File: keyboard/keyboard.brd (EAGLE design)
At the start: 114 x 132 mm, 47 parts, among them SW1 CHERRY_MX, SW10 CHERRY_MX, SW11 CHERRY_MX, SW12 CHERRY_MX, SW13 CHERRY_MX, SW14 CHERRY_MX, SW15 CHERRY_MX, SW16 CHERRY_MX, SW17 CHERRY_MX, SW18 CHERRY_MX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

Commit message: remove airwire
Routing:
- net GND: track 120.1 -> 112.2 mm
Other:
- outline, holes or cut-outs redrawn
- board text removed: "TODO: Make battery hole"
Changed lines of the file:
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@@
 <setting verticaltext="up"/>
 </settings>
-<grid distance="0.1" unitdist="mm" unit="mm" style="lines" multiple="1" display="yes" altdistance="5" altunitdist="mil" altunit="mil"/>
+<grid distance="0.05" unitdist="mm" unit="mm" style="lines" multiple="1" display="yes" altdistance="5" altunitdist="mil" altunit="mil"/>
 <layers>
 <layer number="1" name="Top" color="4" fill="1" visible="yes" active="yes"/>
@@
 <wire x1="94" y1="122.5" x2="95" y2="121.5" width="0.15" layer="20" curve="-90"/>
 <wire x1="95" y1="121.5" x2="95" y2="88" width="0.15" layer="20"/>
-<wire x1="95" y1="88" x2="113" y2="88" width="0.15" layer="20"/>
-<wire x1="113" y1="88" x2="114" y2="87" width="0.15" layer="20" curve="-90"/>
-<wire x1="114" y1="87" x2="114" y2="1" width="0.15" layer="20"/>
+<wire x1="95" y1="88" x2="104.5" y2="88" width="0.15" layer="20"/>
+<wire x1="104.5" y1="88" x2="108.7" y2="83.8" width="0.15" layer="20" curve="-90"/>
+<wire x1="108.7" y1="83.8" x2="108.7" y2="79.75" width="0.15" layer="20"/>
+<wire x1="114" y1="1" x2="114" y2="78.75" width="0.15" layer="20"/>
+<wire x1="114" y1="78.75" x2="113" y2="79.75" width="0.15" layer="20" curve="90"/>
+<wire x1="113" y1="79.75" x2="108.7" y2="79.75" width="0.15" layer="20"/>
 <wire x1="114" y1="1" x2="113" y2="0" width="0.15" layer="20" curve="-90"/>
 <wire x1="113" y1="0" x2="1" y2="0" width="0.15" layer="20"/>
@@
 <wire x1="24.4" y1="2.4" x2="24.4" y2="6.7" width="0.1524" layer="20"/>
 <wire x1="43.4" y1="2.4" x2="43.4" y2="6.7" width="0.1524" layer="20"/>
-<text x="25.4" y="16.5" size="1.778" layer="21">TODO:
-Make battery hole</text>
 <text x="110.1" y="28.3" size="1.016" layer="21" distance="150">5V+
 GND
@@
 <contactref element="U$2" pad="GND"/>
 <contactref element="U$9" pad="GND"/>
-<wire x1="60.3" y1="8" x2="60.3" y2="16.1" width="0.6096" layer="1"/>
+<wire x1="60.3" y1="11.15" x2="60.3" y2="16.1" width="0.6096" layer="1"/>
 <wire x1="60.3" y1="8" x2="60.3" y2="16.1" width="0.6096" layer="16"/>
 <via x="57.3" y="14.1" extent="1-16" drill="0.35"/>
@@
 <wire x1="63.21" y1="10.07" x2="63" y2="10" width="0.127" layer="1"/>
 <wire x1="63.21" y1="10.07" x2="63.3" y2="10.1" width="0.127" layer="1"/>
-<wire x1="61.5" y1="10" x2="61.3" y2="10.1" width="0.127" layer="1"/>
 <wire x1="57.3" y1="12.1" x2="57.5" y2="12" width="0.127" layer="1"/>
 <wire x1="59.3" y1="12.1" x2="59" y2="12" width="0.127" layer="1"/>
@@
 <wire x1="60.3" y1="11.15" x2="57.3" y2="8.15" width="0.6096" layer="1"/>
 <wire x1="57.3" y1="8.15" x2="57.3" y2="8.1" width="0.6096" layer="1"/>
-<wire x1="60.3" y1="11.15" x2="60.3" y2="11.1" width="0.6096" layer="1"/>
-<wire x1="61.25" y1="10.15" x2="60.3" y2="11.1" width="0.6096" layer="1"/>
-<wire x1="61.25" y1="10.15" x2="63.3" y2="8.1" width="0.6096" layer="1"/>
+<wire x1="60.3" y1="11.1" x2="61.3" y2="10.1" width="0.6096" layer="1"/>
+<wire x1="61.3" y1="10.1" x2="63.3" y2="8.1" width="0.6096" layer="1"/>
 <wire x1="60.3" y1="11.15" x2="61.38" y2="10.07" width="0.6096" layer="1"/>
 <wire x1="61.38" y1="10.07" x2="63.21" y2="10.07" width="0.6096" layer="1"/>
@@
 <wire x1="60.3" y1="11.15" x2="60.25" y2="11.15" width="0.6096" layer="1"/>
 <wire x1="60.25" y1="11.15" x2="59.3" y2="12.1" width="0.6096" layer="1"/>
-<wire x1="60.3" y1="11.15" x2="60.3" y2="11.1" width="0.6096" layer="1"/>
 <wire x1="60.3" y1="11.1" x2="59.3" y2="10.1" width="0.6096" layer="1"/>
 <wire x1="60.3" y1="11.15" x2="60.3" y2="11.1" width="0.6096" layer="1"/>
-<wire x1="60.3" y1="11.1" x2="61.25" y2="10.15" width="0.6096" layer="1"/>
-<wire x1="60.3" y1="11.15" x2="61.25" y2="12.1" width="0.6096" layer="1"/>
-<wire x1="61.25" y1="12.1" x2="61.3" y2="12.1" width="0.6096" layer="1"/>
 <wire x1="60.3" y1="11.15" x2="61.3" y2="12.15" width="0.6096" layer="1"/>
 <wire x1="61.3" y1="12.15" x2="61.3" y2="14.1" width="0.6096" layer="1"/>
@@
 <wire x1="60.3" y1="11.15" x2="60.3" y2="11.16" width="0.6096" layer="1"/>
 <wire x1="60.3" y1="11.16" x2="57.42" y2="14.04" width="0.6096" layer="1"/>
-<wire x1="60.3" y1="13.1" x2="60.3" y2="11.15" width="0.6096" layer="16"/>
-<wire x1="60.3" y1="13.1" x2="59.3" y2="14.1" width="0.6096" layer="16"/>
 <wire x1="60.3" y1="11.15" x2="57.35" y2="14.1" width="0.6096" layer="16"/>
 <wire x1="57.35" y1="14.1" x2="57.3" y2="14.1" width="0.6096" layer="16"/>
@@
 <wire x1="60.3" y1="11.15" x2="61.25" y2="12.1" width="0.6096" layer="16"/>
 <wire x1="61.25" y1="12.1" x2="63.3" y2="12.1" width="0.6096" layer="16"/>
-<wire x1="60.3" y1="11.15" x2="61.35" y2="10.1" width="0.6096" layer="16"/>
+<wire x1="61.3" y1="10.15" x2="61.35" y2="10.1" width="0.6096" layer="16"/>
 <wire x1="61.35" y1="10.1" x2="63.3" y2="10.1" width="0.6096" layer="16"/>
-<wire x1="60.3" y1="11.15" x2="59.3" y2="10.15" width="0.6096" layer="16"/>
 <wire x1="59.3" y1="10.15" x2="59.3" y2="10.1" width="0.6096" layer="16"/>
 <wire x1="60.3" y1="11.15" x2="59.3" y2="10.15" width="0.6096" layer="16"/>
-<wire x1="59.3" y1="10.15" x2="59.3" y2="8.1" width="0.6096" layer="16"/>
-<wire x1="60.3" y1="11.15" x2="61.3" y2="10.15" width="0.6096" layer="16"/>
+<wire x1="59.3" y1="10.1" x2="59.3" y2="8.1" width="0.6096" layer="16"/>
 <wire x1="61.3" y1="10.15" x2="61.3" y2="8.1" width="0.6096" layer="16"/>
 <wire x1="60.3" y1="11.15" x2="59.25" y2="10.1" width="0.6096" layer="16"/>
 <wire x1="59.25" y1="10.1" x2="57.3" y2="10.1" width="0.6096" layer="16"/>
-<wire x1="60.3" y1="11.15" x2="57.3" y2="8.15" width="0.6096" layer="16"/>
 <wire x1="57.3" y1="8.15" x2="57.3" y2="8.1" width="0.6096" layer="16"/>
-<wire x1="60.3" y1="11.15" x2="63.3" y2="8.15" width="0.6096" layer="16"/>
+<wire x1="60.3" y1="11.15" x2="61.15" y2="10.3" width="0.6096" layer="16"/>
+<wire x1="61.35" y1="10.1" x2="63.3" y2="8.15" width="0.6096" layer="16"/>
 <wire x1="63.3" y1="8.15" x2="63.3" y2="8.1" width="0.6096" layer="16"/>
-<wire x1="61.3" y1="10.15" x2="61.3" y2="10.1" width="0" layer="19" extent="16-16"/>
+<wire x1="60.3" y1="11.15" x2="60.35" y2="11.15" width="0.508" layer="1"/>
+<wire x1="60.35" y1="11.15" x2="61.3" y2="12.1" width="0.508" layer="1"/>
+<wire x1="60.3" y1="11.15" x2="57.3" y2="8.15" width="0.508" layer="16"/>
+<wire x1="60.3" y1="11.15" x2="59.3" y2="12.15" width="0.508" layer="16"/>
+<wire x1="59.3" y1="12.15" x2="59.3" y2="14.1" width="0.508" layer="16"/>
+<wire x1="60.3" y1="11.15" x2="61.3" y2="10.15" width="0.508" layer="16"/>
 </signal>
 <signal name="SW1">

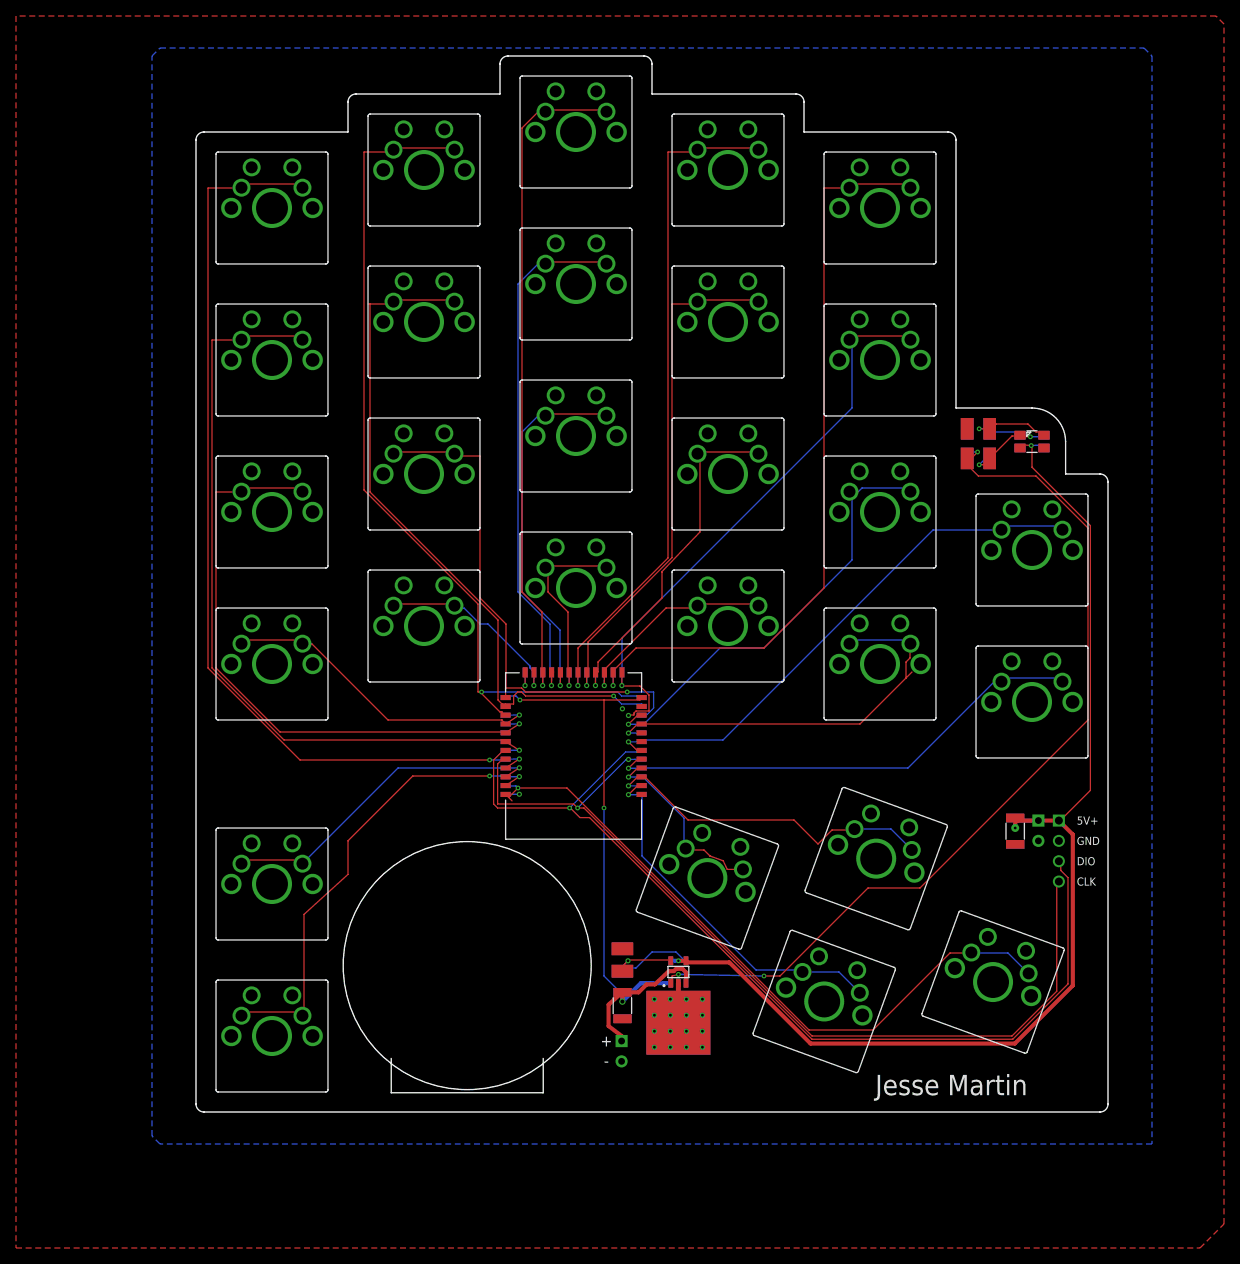
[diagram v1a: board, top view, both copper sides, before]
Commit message: update routing for oshpark
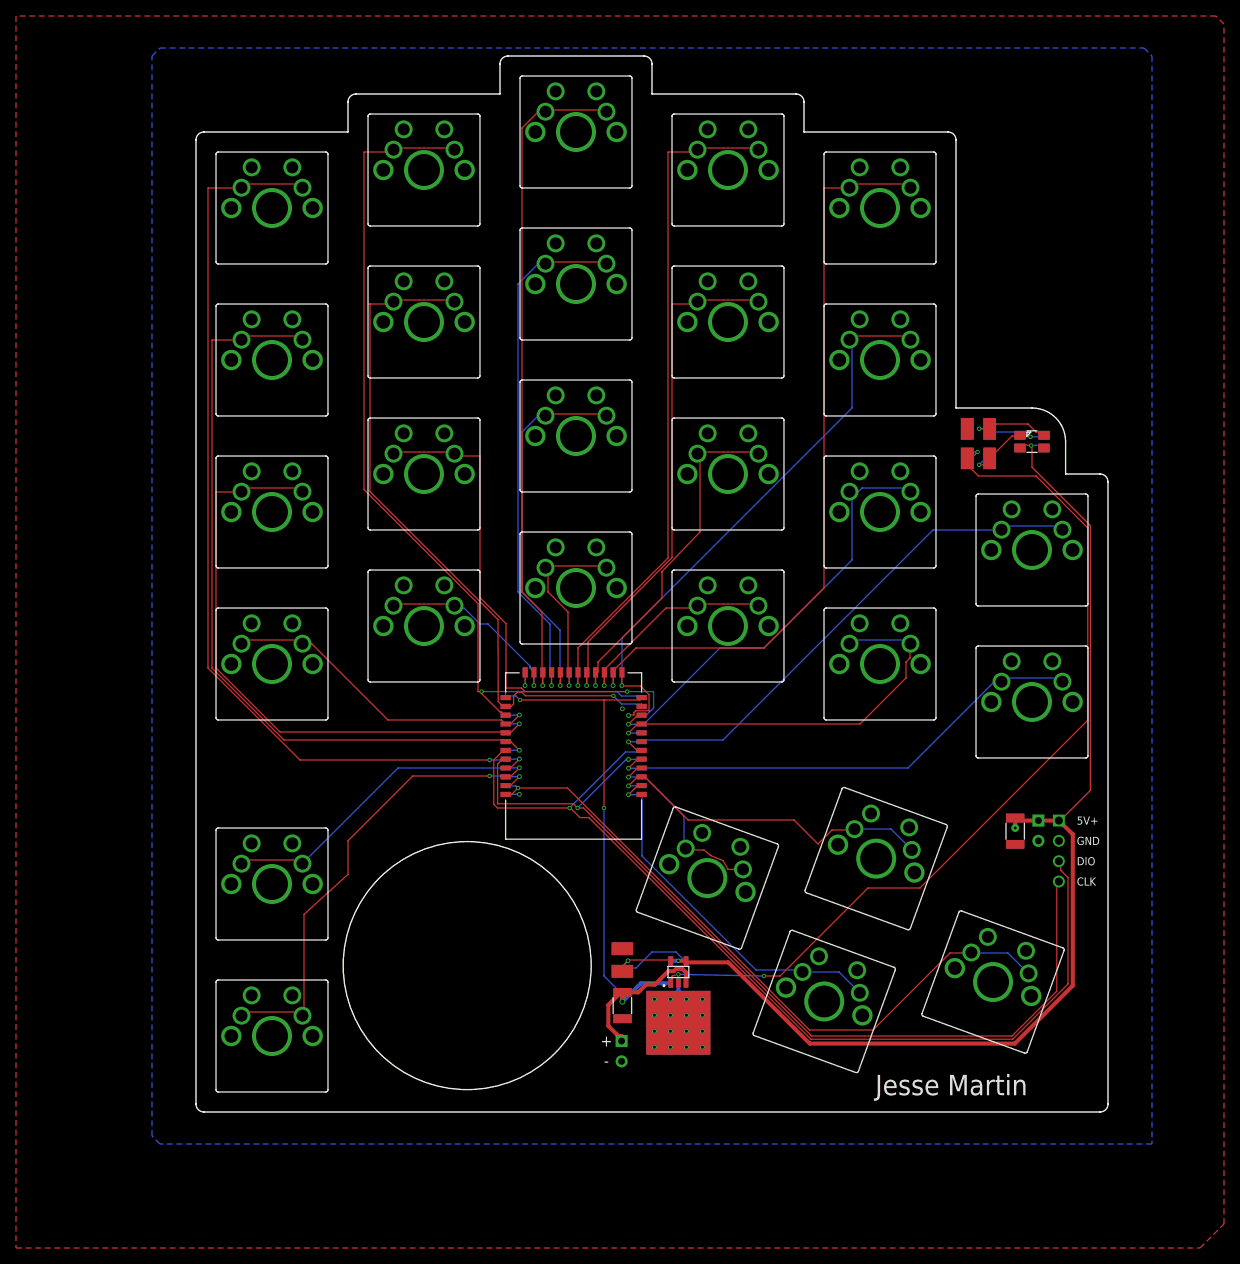
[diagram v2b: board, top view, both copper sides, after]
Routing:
- net GND: track 112.2 -> 48.9 mm
- net SW20: track 52.8 -> 51.8 mm
- net SW28: track 85.9 -> 85.2 mm
- net SW7: track 88.4 -> 87.8 mm
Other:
- outline, holes or cut-outs redrawn

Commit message: update gerbers
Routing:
- net GND: track 48.9 -> 50.4 mm, vias 18 -> 16
- net SWCLK: track 115.1 -> 115.9 mm
- net VCC: track 83.0 -> 83.7 mm
